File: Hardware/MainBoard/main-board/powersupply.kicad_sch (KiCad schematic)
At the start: 28 parts, among them J1 1366005, J2 Conn_01x02, J3 Conn_01x02, SW1 SW_SPST, U1 MCP1727T-3302E/SN

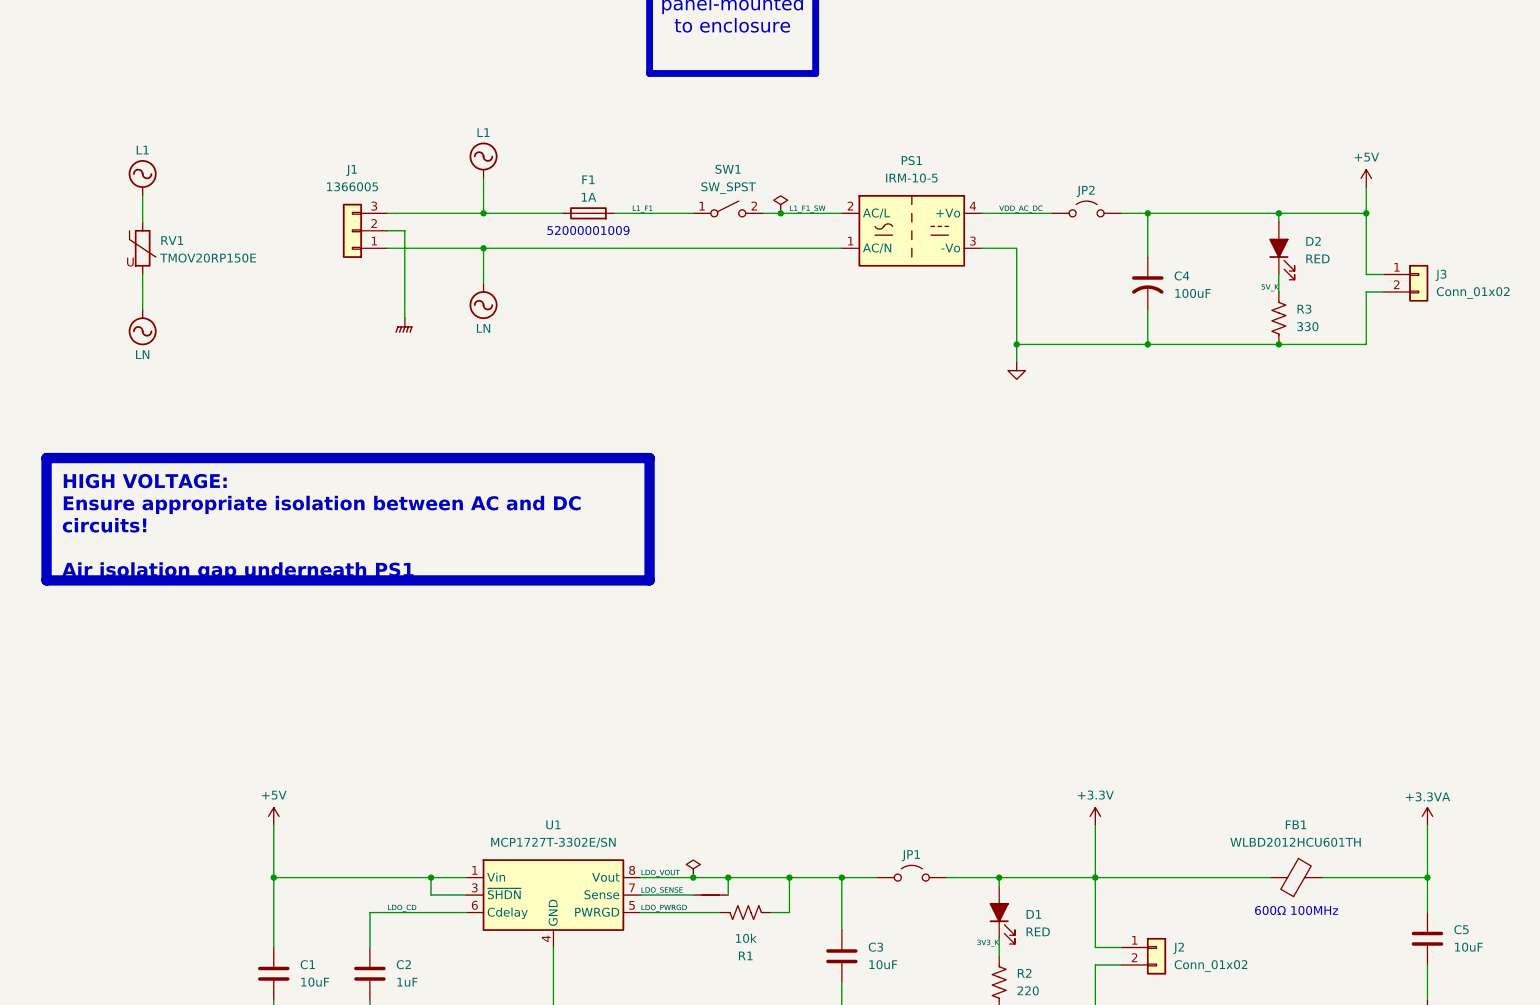
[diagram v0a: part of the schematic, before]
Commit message: edit schematic to pass schematic DRC
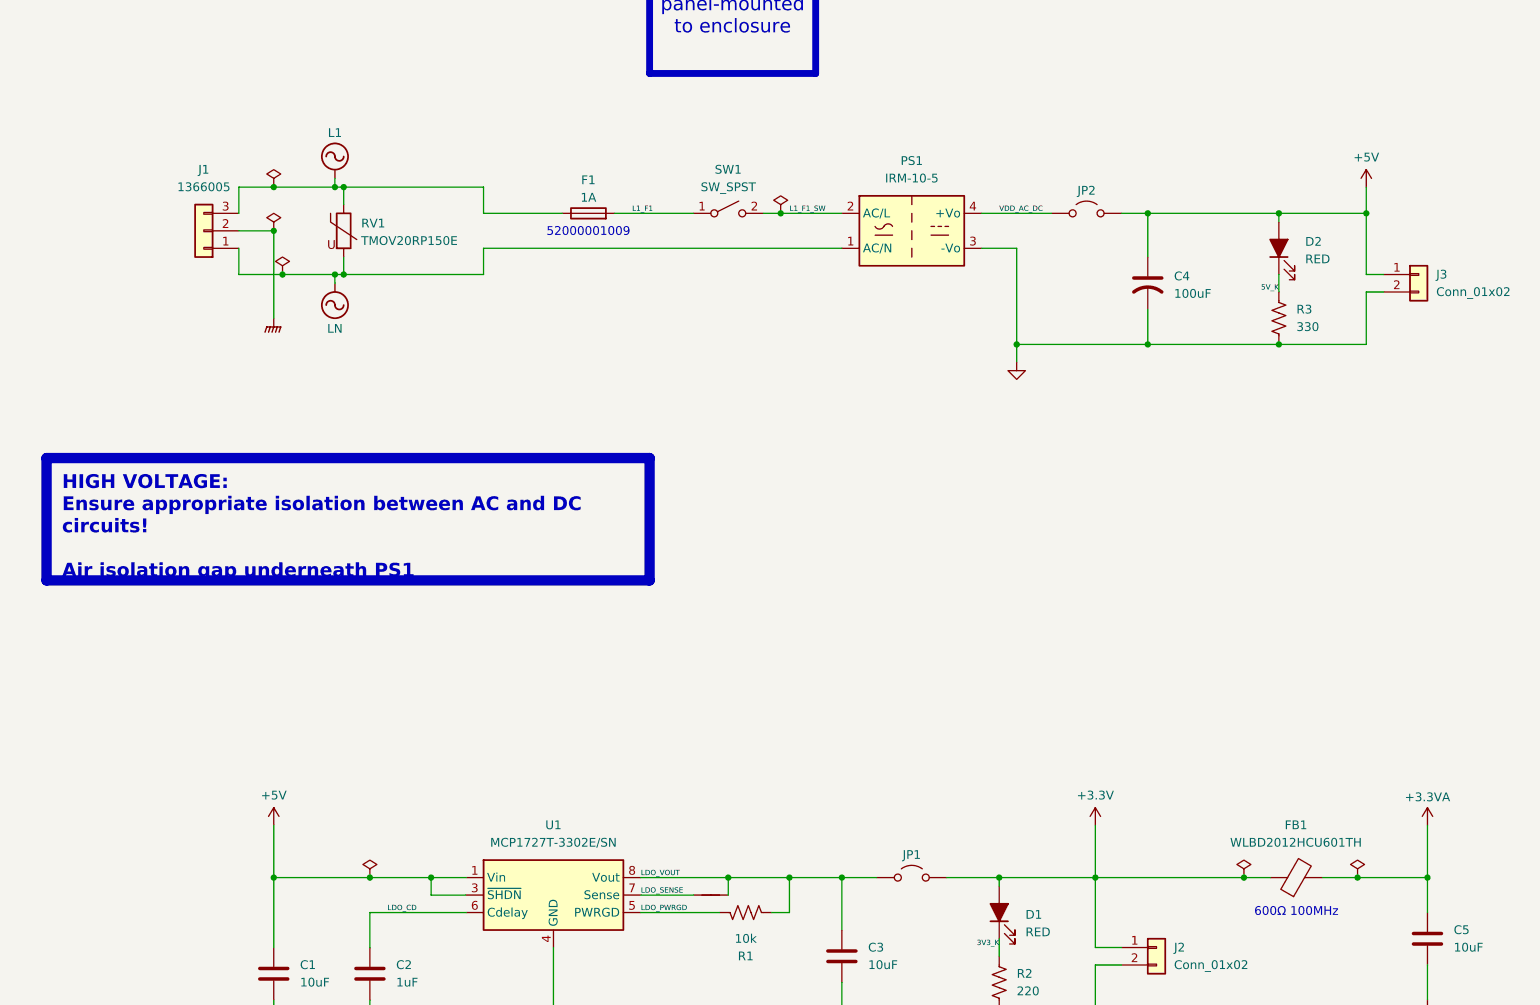
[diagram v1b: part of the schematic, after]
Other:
- moved on the sheet: J1, RV1

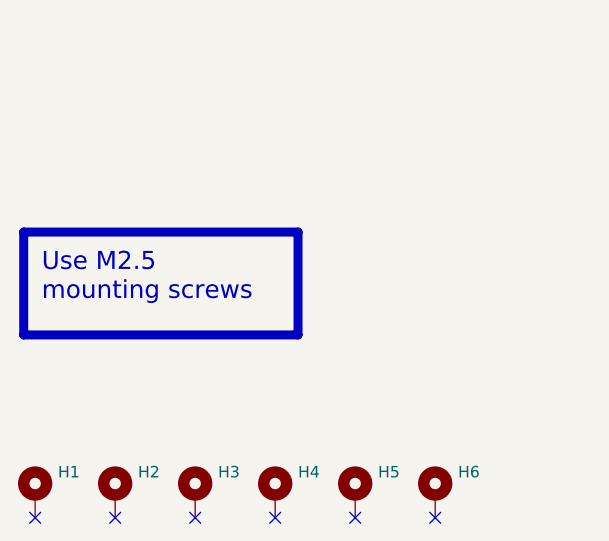
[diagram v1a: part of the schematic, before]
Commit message: add heatsink mounting holes, change a few footprints, clean up schematic
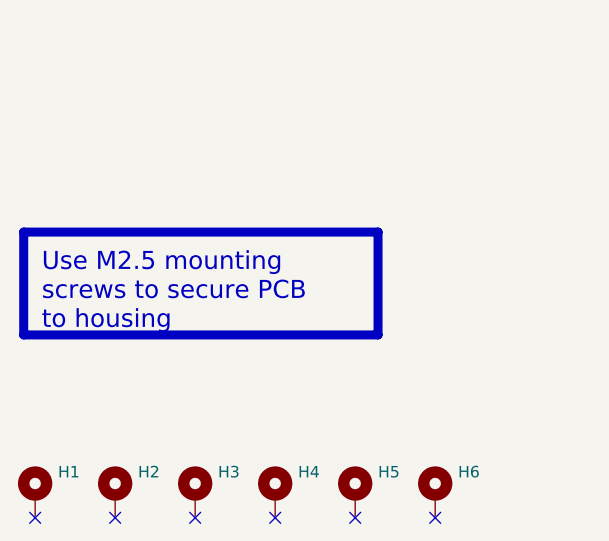
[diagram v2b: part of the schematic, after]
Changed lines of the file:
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@@
 		)
 	)
-	(text_box "Use M2.5 mounting screws"
+	(text_box "Use M2.5 mounting screws to secure PCB to housing"
 		(exclude_from_sim no)
 		(at 33.02 233.68 0)
-		(size 30.48 11.43)
+		(size 39.37 11.43)
 		(margins 2 2 2 2)
 		(stroke

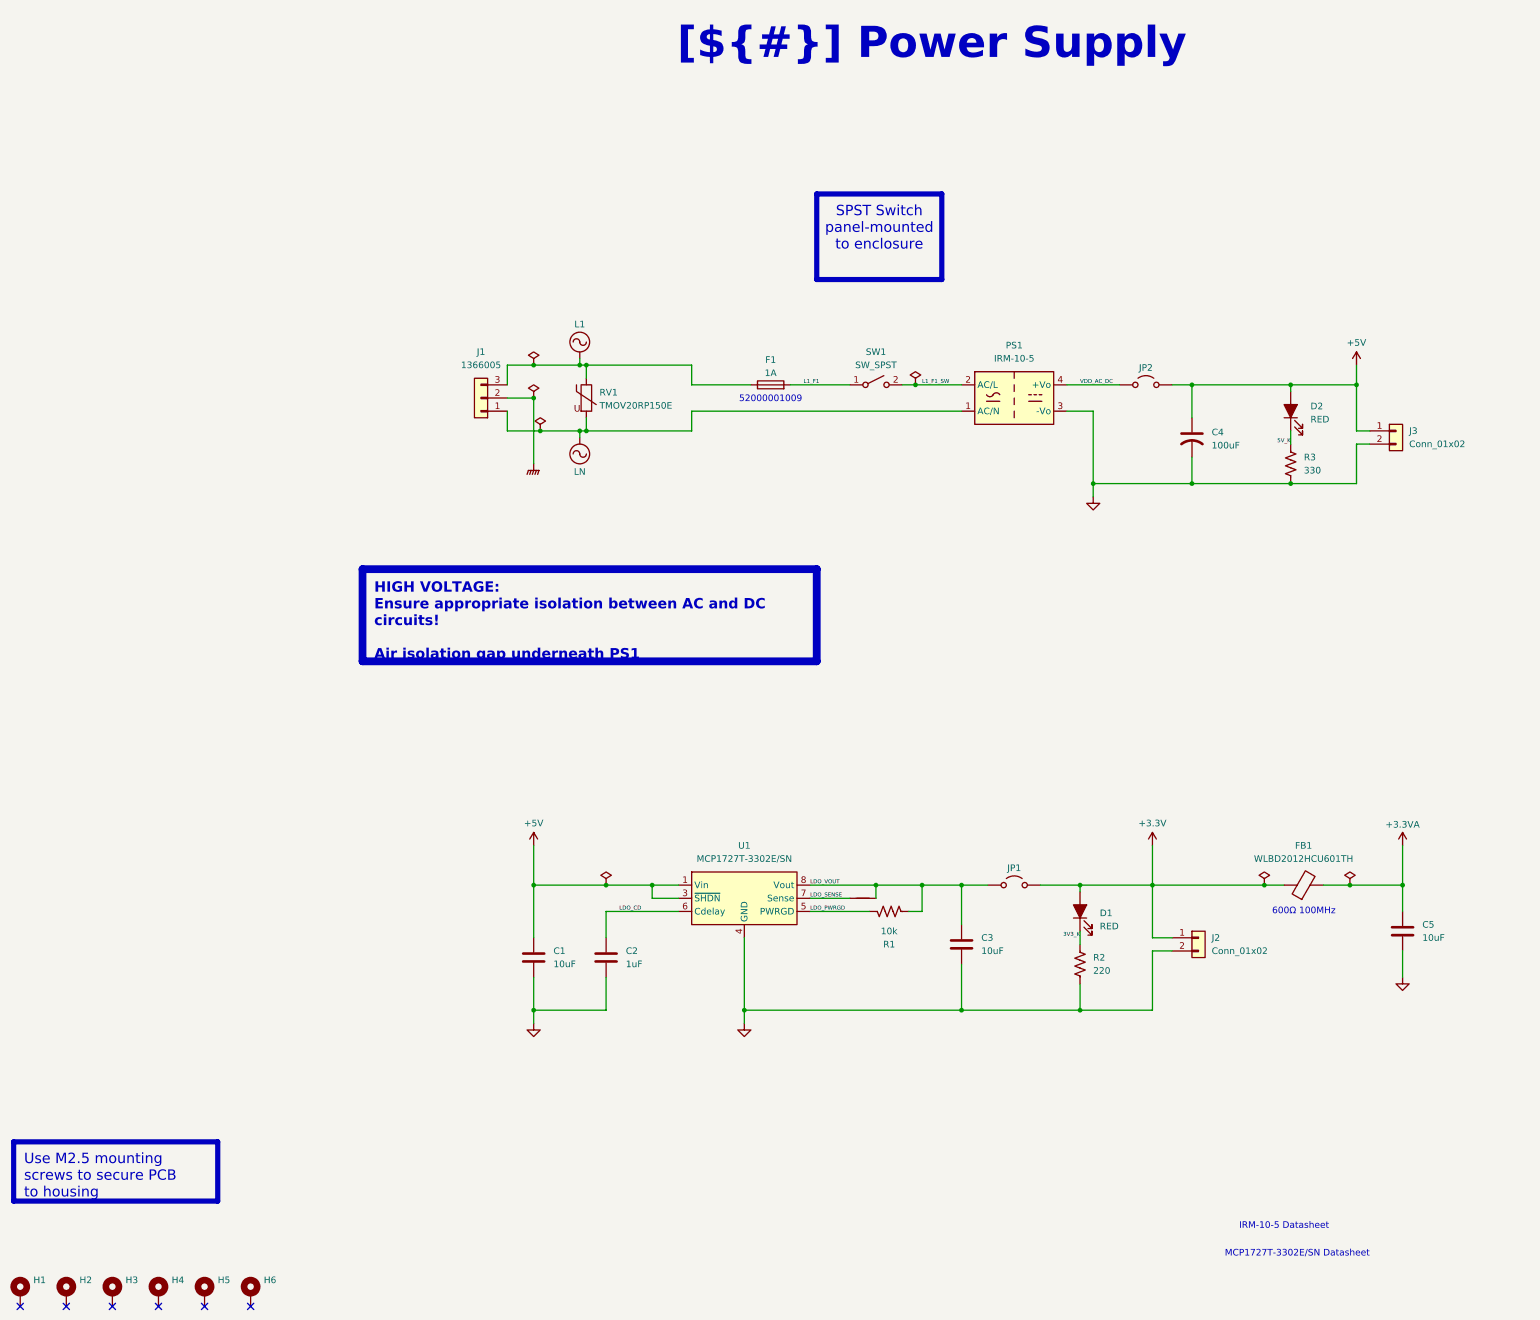
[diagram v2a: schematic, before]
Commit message: add capacitance to 5v power supply
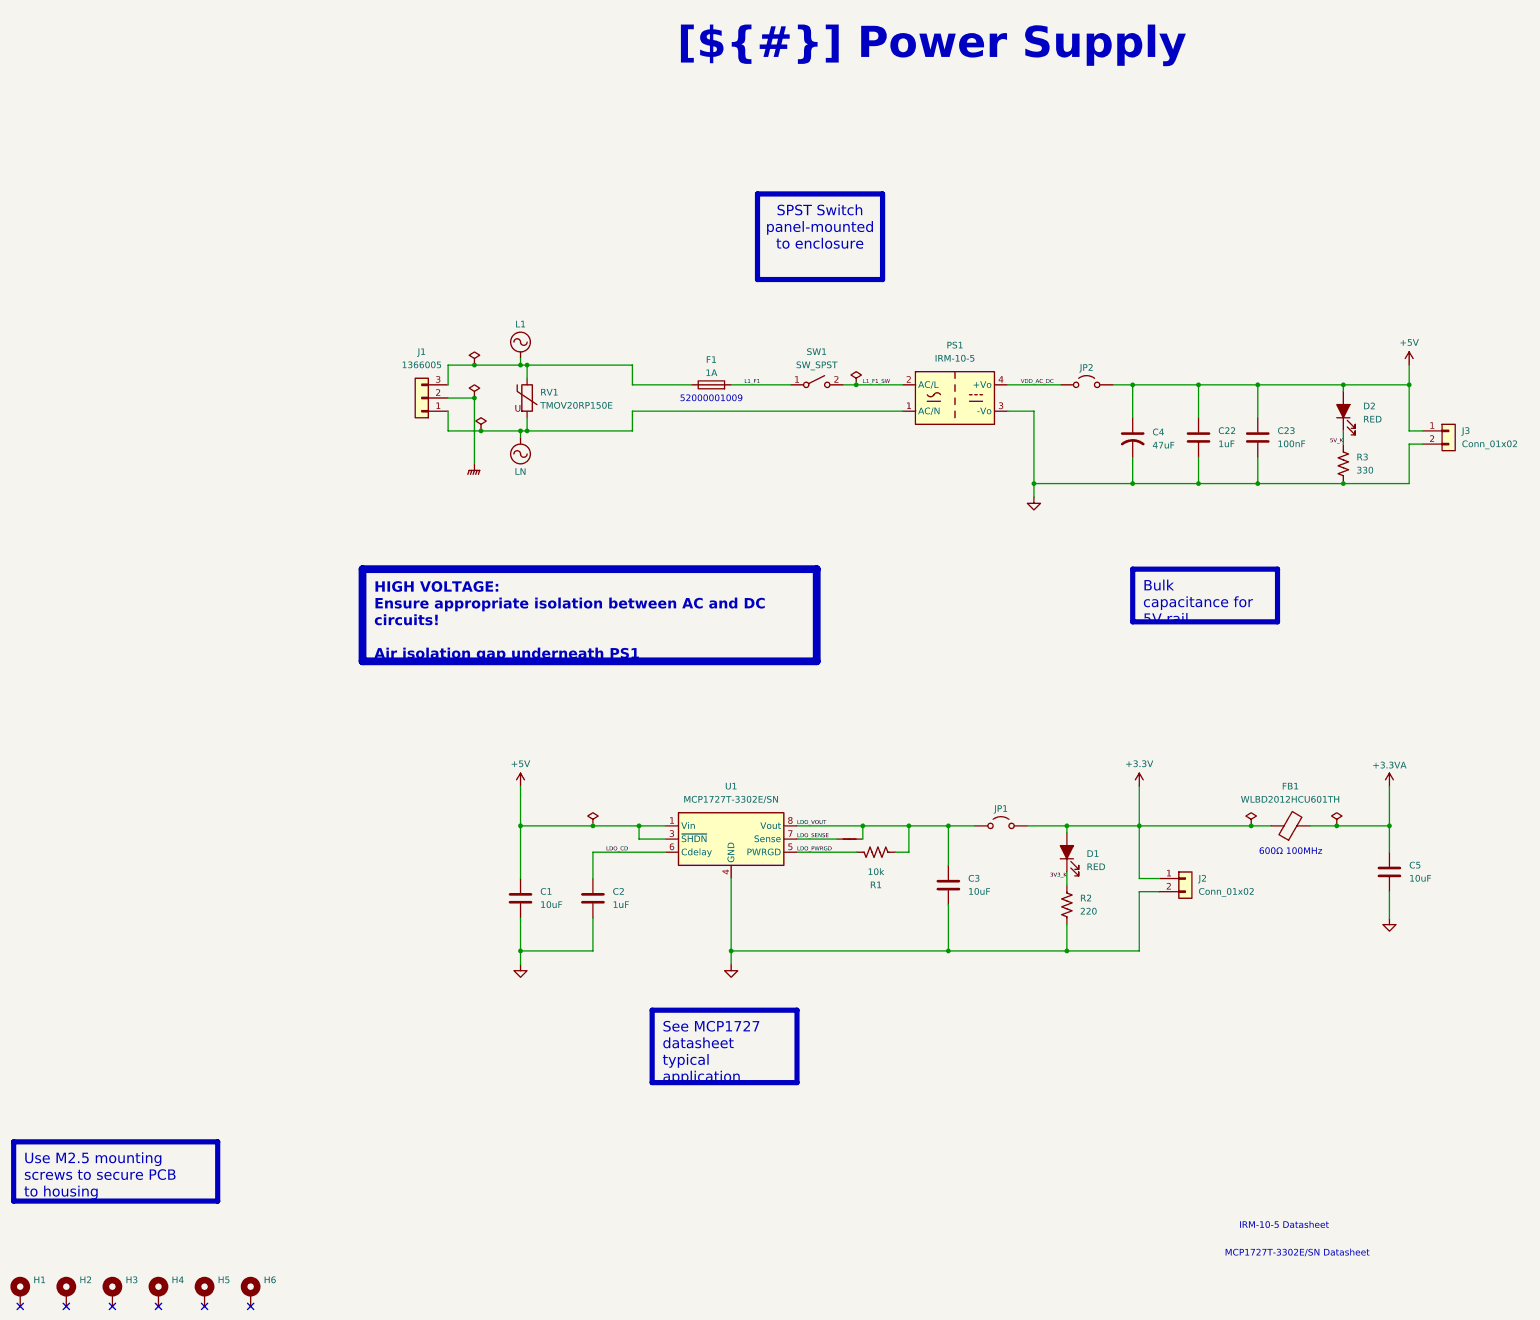
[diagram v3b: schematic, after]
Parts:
- added C22: 1uF, Capacitor_SMD:C_0805_2012Metric_Pad1.18x1.45mm_HandSolder, symbol Device:C
- added C23: 100nF, Capacitor_SMD:C_0603_1608Metric_Pad1.08x0.95mm_HandSolder, symbol Device:C
- C4: value 100uF -> 47uF
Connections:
- net +5V: now also C22.1, C23.1
- net GND: now also C22.2, C23.2
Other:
- moved on the sheet: C1, C2, C3, C4, C5, D1, D2, F1, FB1, J1, J2, J3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

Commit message: Finish board layout
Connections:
- net L1: now also J1.1 (Pin_1); no longer J1.3 (Pin_3)
- net LN: now also J1.3 (Pin_3); no longer J1.1 (Pin_1)
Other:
- moved on the sheet: J1
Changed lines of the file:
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@@
 	(symbol
 		(lib_id "Connector_Generic:Conn_01x03")
-		(at 111.76 90.17 180)
+		(at 111.76 90.17 0)
+		(mirror y)
 		(unit 1)
 		(exclude_from_sim no)
@@
 		(dnp no)
 		(property "Reference" "J1"
-			(at 111.76 81.28 0)
+			(at 111.76 99.06 0)
 			(effects
 				(font
@@
 		)
 		(property "Value" "1366005"
-			(at 111.76 83.82 0)
+			(at 111.76 96.52 0)
 			(effects
 				(font
